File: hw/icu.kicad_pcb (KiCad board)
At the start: 2 copper layers, 60 x 90 mm, 105 parts, among them J1001 ARM_JTAG_SWD_HEADER_10_PINSMD, J101 AMPSEAL_8_POS_VERT_BLACK_SEAL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, J102 AMPSEAL_23_POS_VERT_GRAY_SEAL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, U1001 MCP2551_SOIC8, U1002 LPC1549JBD64, U301 VND5050AJTR-E, U401 VND5050AJTR-E, U501 VND5050AJTR-E, U601 VND5050AJTR-E, U701 VND5050AJTR-E, U801 VND5050AJTR-E, U901 VND5050AJTR-E, X1001 XTAL_7A-12.000MAAJ-T

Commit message: hw 1.0 ready to order
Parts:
- removed F102: FUSE_MC36211_350MA, usevolt:FUSE_MC36211
- removed R101: R_75OHM, usevolt:1206
- added D1401: DIODE_RS07J-GS18, usevolt:DO219AB, F.Cu at (182.2, 52.8)
- added R1401: 10K, yageo:0603, F.Cu at (181.4, 57.0)
- added R1402: 20K, yageo:0603, F.Cu at (183.0, 57.0)
- added R907: 1K, yageo:0603, F.Cu at (166.0, 56.9)
- R902: value e1K -> 1K
- moved F101 8.21 mm to (186.9, 69.0)
- moved R1101 4.10 mm to (169.3, 57.0)
- moved R1201 4.10 mm to (173.3, 57.0)
- moved R1301 4.10 mm to (177.3, 57.0)
- moved D1101 4.10 mm to (170.1, 52.8)
- moved D1201 4.10 mm to (174.1, 52.8)
- moved D1301 4.10 mm to (178.1, 52.8)
- moved R1102 4.10 mm to (170.9, 57.0)
- moved R1202 4.10 mm to (174.9, 57.0)
- moved R1302 4.10 mm to (178.9, 57.0)
- moved X1001 0.94 mm to (150.0, 108.3)
- moved C1008 0.94 mm to (147.3, 106.4)
- moved eC1009 0.94 mm to (147.3, 110.0)
- renumbered C1009 to eC1009
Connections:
- J102 pad 23: Net-(F102-PadP$2) -> /5V_OUT
- J102 pad 4: /Sheet5A7E031D/VIN -> /lpc1549/DIN4
- J102 pad 5: /Sheet5A7E2A6D/VIN -> /Sheet5A7E031D/VIN
- J102 pad 6: /Sheet5A7E34B9/VIN -> /Sheet5A7E2A6D/VIN
- J102 pad 7: Net-(J102-Pad7) -> /Sheet5A7E34B9/VIN
- J102 pad 8: /5V_OUT -> /Sheet5A8C5347/VIN
- U1002 pad P$1: /lpc1549/OUT2_SENSE -> Net-(R904-Pad1)
- U1002 pad P$10: /Sheet5A7B341A/IN1 -> /Sheet5A7B4C12/IN2
- U1002 pad P$11: /lpc1549/AIN3 -> /lpc1549/OUT6_SENSE
- U1002 pad P$12: (no net) -> /lpc1549/OUT7_SENSE
- U1002 pad P$15: Net-(R904-Pad1) -> (no net)
- U1002 pad P$16: Net-(R905-Pad1) -> /Sheet5A7B753C/IN2
- U1002 pad P$17: /Sheet5A7B577D/IN1 -> /Sheet5A7B753C/IN1
- U1002 pad P$19: /Sheet5A7B577D/IN2 -> /Sheet5A7B577D/IN1
- U1002 pad P$2: /Sheet5A7B2C1A/IN2 -> /Sheet5A7B341A/IN2
- U1002 pad P$23: Net-(R906-Pad1) -> (no net)
- U1002 pad P$24: /Sheet5A7B753C/IN1 -> /Sheet5A7B577D/IN2
- U1002 pad P$29: /lpc1549/OUT4_SENSE -> (no net)
- U1002 pad P$3: /lpc1549/OUT1_SENSE -> /lpc1549/AIN4
- U1002 pad P$30: /Sheet5A7B341A/IN2 -> /Sheet5A7B4C12/IN1
- U1002 pad P$31: /lpc1549/OUT6_SENSE -> /lpc1549/OUT3_SENSE
- U1002 pad P$32: /lpc1549/OUT7_SENSE -> /lpc1549/OUT4_SENSE
- U1002 pad P$33: (no net) -> /lpc1549/OUT2_SENSE
- U1002 pad P$34: (no net) -> /lpc1549/OUT1_SENSE
- U1002 pad P$4: /lpc1549/OUT3_SENSE -> /lpc1549/AIN3
- U1002 pad P$5: /Sheet5A7B1579/IN1 -> /Sheet5A7B341A/IN1
- U1002 pad P$51: (no net) -> Net-(R907-Pad2)
- U1002 pad P$53: /Sheet5A7B3FAC/IN1 -> /Sheet5A7B1579/IN2
- U1002 pad P$58: /Sheet5A7B3FAC/IN2 -> /Sheet5A7B1579/IN1
- U1002 pad P$6: /Sheet5A7B1579/IN2 -> /Sheet5A7B3FAC/IN2
- U1002 pad P$61: /Sheet5A7B4C12/IN1 -> /Sheet5A7B2C1A/IN2
- U1002 pad P$62: /Sheet5A7B753C/IN2 -> Net-(R906-Pad1)
- U1002 pad P$63: (no net) -> Net-(R905-Pad1)
- U1002 pad P$64: /Sheet5A7B4C12/IN2 -> /Sheet5A7B2C1A/IN1
- U1002 pad P$7: /Sheet5A7B2C1A/IN1 -> /Sheet5A7B3FAC/IN1
- U1002 pad P$8: /lpc1549/AIN1 -> /lpc1549/AIN2
- U1002 pad P$9: /lpc1549/AIN2 -> /lpc1549/AIN1
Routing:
- net GND: track 98.4 -> 658.2 mm, vias 47 -> 96
- net /lpc1549/AIN4: track 0.00 -> 117.1 mm, vias 0 -> 2
- net /lpc1549/AIN3: track 3.20 -> 108.9 mm, vias 0 -> 2
- net /lpc1549/AIN2: track 3.20 -> 103.3 mm, vias 0 -> 2
- net Net-(R906-Pad1): track 0.00 -> 95.5 mm, vias 0 -> 2
- net Net-(R907-Pad2): track 0.00 -> 95.0 mm, vias 0 -> 2
- net /lpc1549/AIN1: track 3.20 -> 97.2 mm, vias 0 -> 2
- net Net-(R905-Pad1): track 0.00 -> 92.2 mm, vias 0 -> 2
- net Net-(R904-Pad1): track 0.00 -> 88.8 mm, vias 0 -> 2
- net /lpc1549/OUT7_SENSE: track 10.5 -> 65.7 mm, vias 0 -> 2
- net /Sheet5A7B753C/IN2: track 2.88 -> 52.4 mm, vias 0 -> 2
- net /Sheet5A7B753C/IN1: track 2.53 -> 51.8 mm, vias 0 -> 2
- net /lpc1549/OUT6_SENSE: track 10.7 -> 59.9 mm, vias 0 -> 2
- net /Sheet5A7B4C12/IN2: track 2.91 -> 51.5 mm, vias 0 -> 2
- net /Sheet5A7B577D/IN1: track 2.50 -> 49.9 mm, vias 0 -> 2
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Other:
- net class Default: clearance 0.2 -> 0.199
- rule trace_clearance: 0.2 -> 0.199

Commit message: 3.0.0 hw and gerber created
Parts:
- removed C203: 10nF, kemet:0603
- removed D301, D401, D501, D601, D701, D801, D901: DIODE_RS07J-GS18, usevolt:DO219AB
- removed R303, R403, R503, R603, R703, R803, R903: 390, yageo:0603
- removed VR202: REG_MCP1700, usevolt:SOT-23_3-PIN
- removed eC1009: 18pF, kemet:0603
- added C1: 100nF, kemet:0603, F.Cu at (162.2, 131.4)
- added C1009: 18pF, kemet:0603, F.Cu at (147.3, 110.0)
- added D1: ZENER_MM3Z3V6T1G, usevolt:SOD-323, F.Cu at (155.1, 97.8)
- added D2: ZENER_MM3Z3V6T1G, usevolt:SOD-323, F.Cu at (162.5, 97.8)
- added D3: ZENER_MM3Z3V6T1G, usevolt:SOD-323, F.Cu at (167.7, 97.8)
- added D4: ZENER_MM3Z3V6T1G, usevolt:SOD-323, F.Cu at (174.6, 97.8)
- added D5: ZENER_MM3Z3V6T1G, usevolt:SOD-323, F.Cu at (180.8, 97.8)
- added D6: ZENER_MM3Z3V6T1G, usevolt:SOD-323, F.Cu at (186.9, 97.8)
- added D7: ZENER_MM3Z3V6T1G, usevolt:SOD-323, F.Cu at (148.5, 97.8)
- added R1: 1K, yageo:0603, F.Cu at (156.2, 93.8)
- added R2: 1K, yageo:0603, F.Cu at (162.6, 93.8)
- added R3: 1K, yageo:0603, F.Cu at (169.0, 93.8)
- added R4: 1K, yageo:0603, F.Cu at (175.4, 93.8)
- added R5: 1K, yageo:0603, F.Cu at (181.8, 93.8)
- added R6: 1K, yageo:0603, F.Cu at (188.2, 93.8)
- added R7: 1K, yageo:0603, F.Cu at (149.8, 93.8)
- added VR1: REG_MCP1700, usevolt:SOT-23_3-PIN, F.Cu at (141.7, 135.7)
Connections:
- J1001 pad P$6: (no net) -> Net-(J1001-PadP$6)
- J1001 pad P$7: (no net) -> Net-(J1001-PadP$7)
- J1001 pad P$8: (no net) -> Net-(J1001-PadP$8)
- J101 pad 7: (no net) -> Net-(J101-Pad7)
- J101 pad 8: (no net) -> Net-(J101-Pad8)
- U1001 pad 5: (no net) -> Net-(U1001-Pad5)
- U1002 pad P$15: (no net) -> Net-(U1002-PadP$15)
- U1002 pad P$23: (no net) -> Net-(U1002-PadP$23)
- U1002 pad P$25: (no net) -> Net-(U1002-PadP$25)
- U1002 pad P$29: (no net) -> Net-(U1002-PadP$29)
- U1002 pad P$38: (no net) -> Net-(U1002-PadP$38)
- U1002 pad P$39: (no net) -> Net-(U1002-PadP$39)
- U1002 pad P$42: (no net) -> Net-(U1002-PadP$42)
- U1002 pad P$43: (no net) -> Net-(U1002-PadP$43)
- U1002 pad P$46: (no net) -> Net-(U1002-PadP$46)
- U1002 pad P$47: (no net) -> Net-(U1002-PadP$47)
- U1002 pad P$48: (no net) -> Net-(U1002-PadP$48)
- U1002 pad P$49: (no net) -> Net-(U1002-PadP$49)
- U1002 pad P$50: (no net) -> Net-(U1002-PadP$50)
- U1002 pad P$54: (no net) -> Net-(U1002-PadP$54)
- U301 pad 6: (no net) -> Net-(U301-Pad6)
- U401 pad 6: (no net) -> Net-(U401-Pad6)
- U501 pad 6: (no net) -> Net-(U501-Pad6)
- U601 pad 6: (no net) -> Net-(U601-Pad6)
- U701 pad 6: (no net) -> Net-(U701-Pad6)
- U801 pad 6: (no net) -> Net-(U801-Pad6)
- U901 pad 6: (no net) -> Net-(U901-Pad6)
- VR201 pad 2: (no net) -> Net-(VR201-Pad2)
- VR201 pad 3: (no net) -> Net-(VR201-Pad3)
- VR201 pad 5: (no net) -> Net-(VR201-Pad5)
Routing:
- net +3V3: track 230.6 -> 177.2 mm, vias 2 -> 0
- net GND: track 658.2 -> 681.7 mm
- net /lpc1549/OUT4_SENSE: track 39.7 -> 41.0 mm
- net /lpc1549/OUT7_SENSE: track 65.7 -> 67.0 mm
- net /lpc1549/OUT2_SENSE: track 33.8 -> 35.1 mm
- net /lpc1549/OUT5_SENSE: track 44.9 -> 46.1 mm
- net /lpc1549/OUT6_SENSE: track 59.9 -> 61.1 mm
- net /lpc1549/OUT3_SENSE: track 38.7 -> 39.8 mm
- net /lpc1549/OUT1_SENSE: track 31.9 -> 32.9 mm
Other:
- board text added: "UW ISB 3.0 Usevolt Oy"
- board text removed: "UW ISB 1.0 Usevolt Oy"

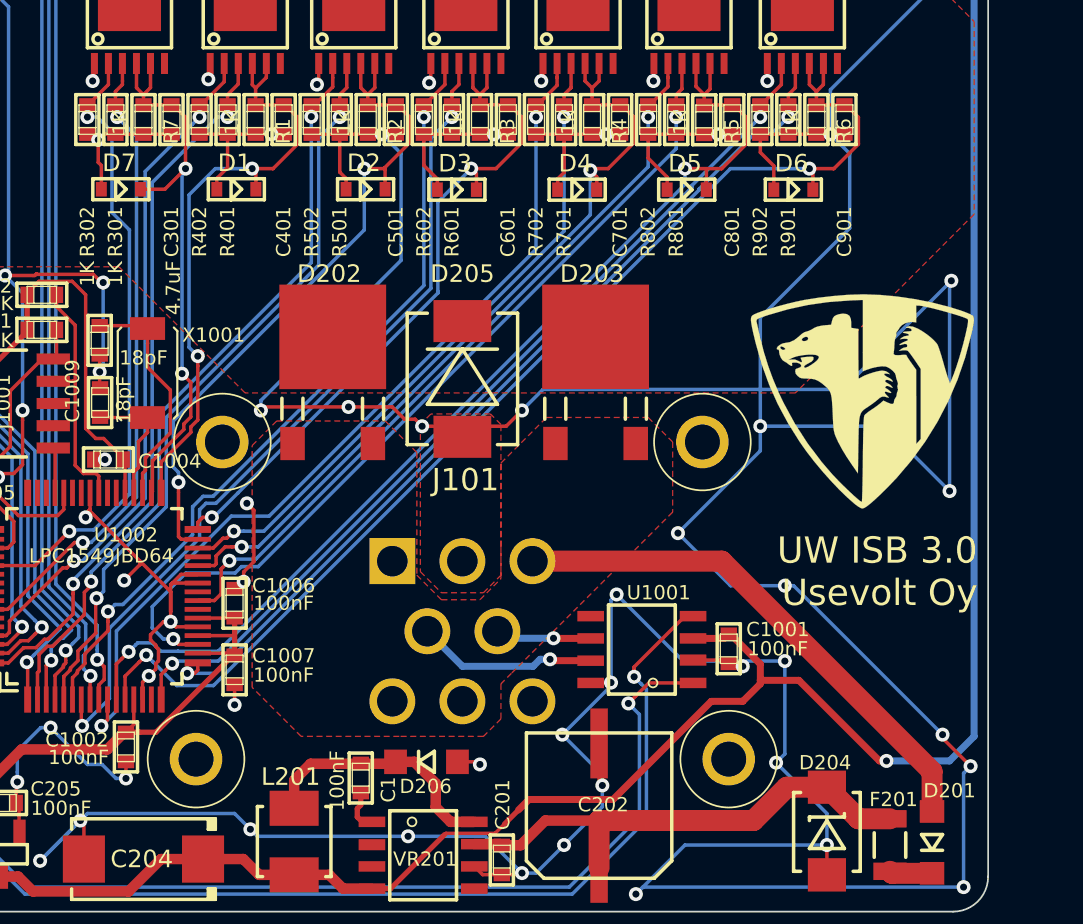
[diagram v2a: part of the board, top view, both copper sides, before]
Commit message: hw 3.1 silkscreen modifications
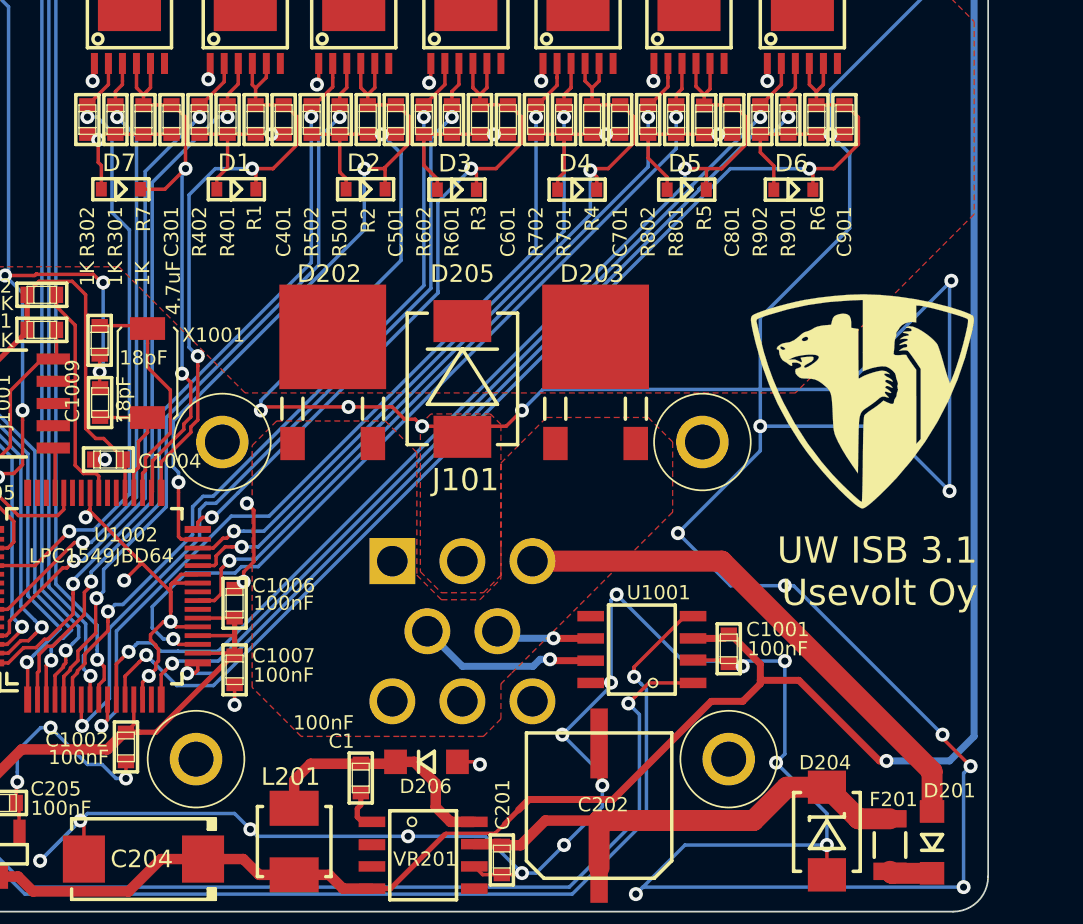
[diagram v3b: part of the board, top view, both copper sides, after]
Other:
- board text added: "UW ISB 3.1 Usevolt Oy"
- board text removed: "UW ISB 3.0 Usevolt Oy"
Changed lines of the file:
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@@
     (at 162.2 131.375 270)
     (attr smd)
-    (fp_text reference C1 (at 0.6604 -1.5748 270) (layer F.SilkS)
-      (effects (font (size 0.8128 0.8128) (thickness 0.0762)))
-    )
-    (fp_text value 100nF (at 0.1524 1.3462 270) (layer F.SilkS)
+    (fp_text reference C1 (at -2.1 1.1) (layer F.SilkS)
+      (effects (font (size 0.8128 0.8128) (thickness 0.0762)))
+    )
+    (fp_text value 100nF (at -3.15 2.125) (layer F.SilkS)
       (effects (font (size 0.8128 0.8128) (thickness 0.0762)))
     )
@@
     (at 156.2 93.8 270)
     (attr smd)
-    (fp_text reference R1 (at 0.6604 -1.5748 270) (layer F.SilkS)
-      (effects (font (size 0.8128 0.8128) (thickness 0.0762)))
-    )
-    (fp_text value 1K (at 0.1524 1.3462 270) (layer F.SilkS)
+    (fp_text reference R1 (at 5.6 0.075 270) (layer F.SilkS)
+      (effects (font (size 0.8128 0.8128) (thickness 0.0762)))
+    )
+    (fp_text value 1K (at 7.875 0.125 270) (layer F.SilkS) hide
       (effects (font (size 0.8128 0.8128) (thickness 0.0762)))
     )
@@
     (at 162.6 93.8 270)
     (attr smd)
-    (fp_text reference R2 (at 0.6604 -1.5748 270) (layer F.SilkS)
-      (effects (font (size 0.8128 0.8128) (thickness 0.0762)))
-    )
-    (fp_text value 1K (at 0.1524 1.3462 270) (layer F.SilkS)
+    (fp_text reference R2 (at 5.75 -0.025 270) (layer F.SilkS)
+      (effects (font (size 0.8128 0.8128) (thickness 0.0762)))
+    )
+    (fp_text value 1K (at 0.1524 1.3462 270) (layer F.SilkS) hide
       (effects (font (size 0.8128 0.8128) (thickness 0.0762)))
     )
@@
     (at 169 93.8 270)
     (attr smd)
-    (fp_text reference R3 (at 0.6604 -1.5748 270) (layer F.SilkS)
-      (effects (font (size 0.8128 0.8128) (thickness 0.0762)))
-    )
-    (fp_text value 1K (at 0.1524 1.3462 270) (layer F.SilkS)
+    (fp_text reference R3 (at 5.625 0.075 270) (layer F.SilkS)
+      (effects (font (size 0.8128 0.8128) (thickness 0.0762)))
+    )
+    (fp_text value 1K (at 0.1524 1.3462 270) (layer F.SilkS) hide
       (effects (font (size 0.8128 0.8128) (thickness 0.0762)))
     )
@@
     (at 175.4 93.8 270)
     (attr smd)
-    (fp_text reference R4 (at 0.6604 -1.5748 270) (layer F.SilkS)
-      (effects (font (size 0.8128 0.8128) (thickness 0.0762)))
-    )
-    (fp_text value 1K (at 0.1524 1.3462 270) (layer F.SilkS)
+    (fp_text reference R4 (at 5.65 0 270) (layer F.SilkS)
+      (effects (font (size 0.8128 0.8128) (thickness 0.0762)))
+    )
+    (fp_text value 1K (at 0.1524 1.3462 270) (layer F.SilkS) hide
       (effects (font (size 0.8128 0.8128) (thickness 0.0762)))
     )
@@
     (at 181.8 93.8118 270)
     (attr smd)
-    (fp_text reference R5 (at 0.6604 -1.5748 270) (layer F.SilkS)
-      (effects (font (size 0.8128 0.8128) (thickness 0.0762)))
-    )
-    (fp_text value 1K (at 0.1524 1.3462 270) (layer F.SilkS)
+    (fp_text reference R5 (at 5.5882 0 270) (layer F.SilkS)
+      (effects (font (size 0.8128 0.8128) (thickness 0.0762)))
+    )
+    (fp_text value 1K (at 0.1524 1.3462 270) (layer F.SilkS) hide
       (effects (font (size 0.8128 0.8128) (thickness 0.0762)))
     )
@@
     (at 188.2 93.8 270)
     (attr smd)
-    (fp_text reference R6 (at 0.6604 -1.5748 270) (layer F.SilkS)
-      (effects (font (size 0.8128 0.8128) (thickness 0.0762)))
-    )
-    (fp_text value 1K (at 0.1524 1.3462 270) (layer F.SilkS)
+    (fp_text reference R6 (at 5.625 -0.1 270) (layer F.SilkS)
+      (effects (font (size 0.8128 0.8128) (thickness 0.0762)))
+    )
+    (fp_text value 1K (at 0.1524 1.3462 270) (layer F.SilkS) hide
       (effects (font (size 0.8128 0.8128) (thickness 0.0762)))
     )
@@
     (at 149.8 93.8 270)
     (attr smd)
-    (fp_text reference R7 (at 0.6604 -1.5748 270) (layer F.SilkS)
-      (effects (font (size 0.8128 0.8128) (thickness 0.0762)))
-    )
-    (fp_text value 1K (at 0.1524 1.3462 270) (layer F.SilkS)
+    (fp_text reference R7 (at 5.675 0 270) (layer F.SilkS)
+      (effects (font (size 0.8128 0.8128) (thickness 0.0762)))
+    )
+    (fp_text value 1K (at 8.8 0.05 270) (layer F.SilkS)
       (effects (font (size 0.8128 0.8128) (thickness 0.0762)))
     )
@@
     (arrow2b (pts (xy 209.747154 49.003578) (xy 210.333575 50.130082)))
   )
-  (gr_text "UW ISB 3.0\nUsevolt Oy" (at 197.4 119.6) (layer F.SilkS)
+  (gr_text "UW ISB 3.1\nUsevolt Oy" (at 197.4 119.6) (layer F.SilkS)
     (effects (font (size 1.5 1.5) (thickness 0.3)) (justify right))
   )

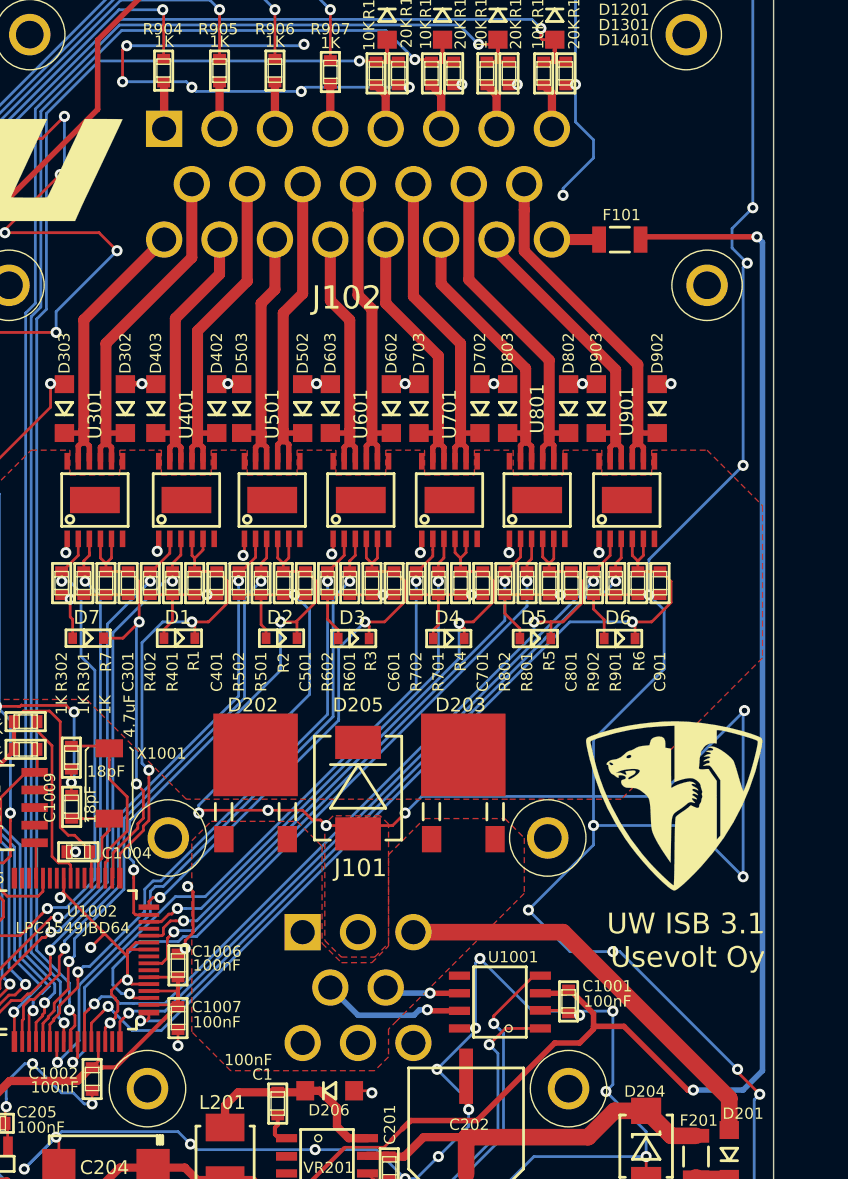
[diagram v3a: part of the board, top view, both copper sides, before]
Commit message: pcb 3.2.0 created, with 12V supply for sensors
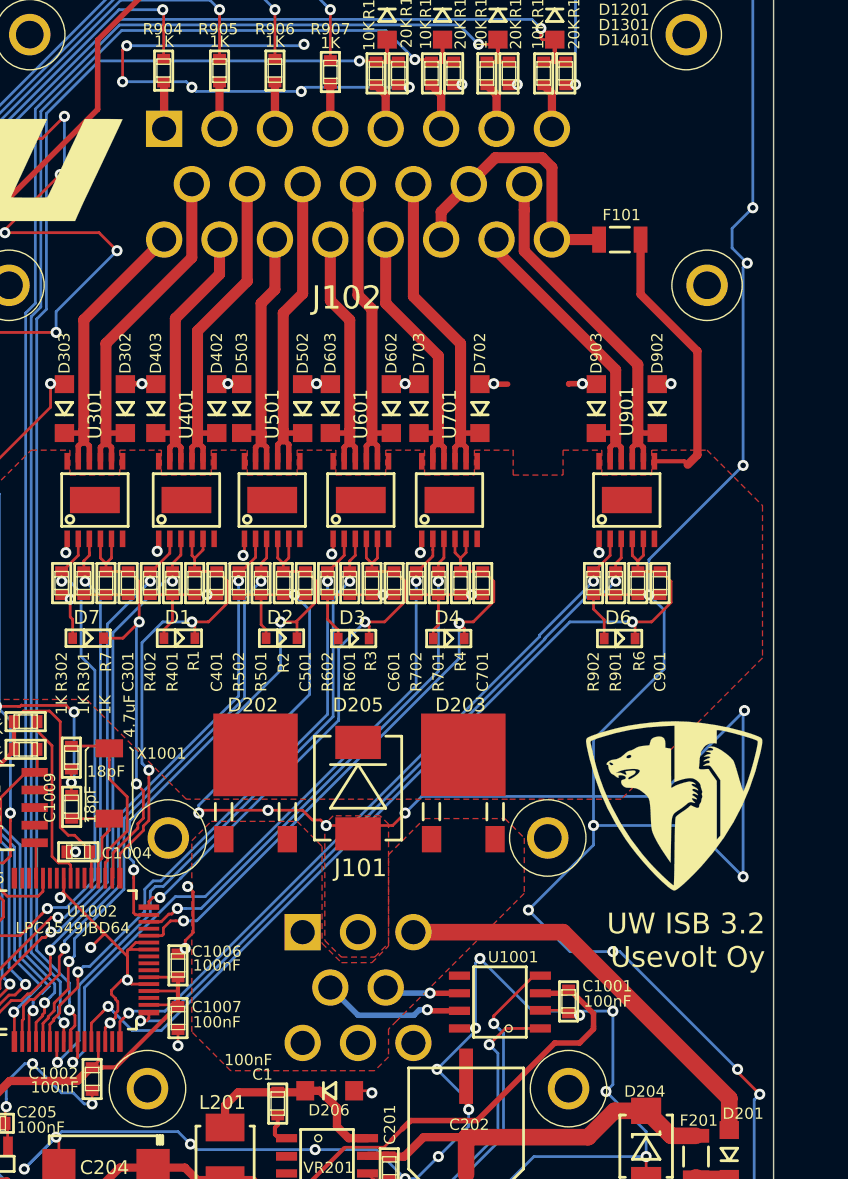
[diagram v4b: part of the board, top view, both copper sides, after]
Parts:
- removed C801: 4.7uF, kemet:0603
- removed D5: ZENER_MM3Z3V6T1G, usevolt:SOD-323
- removed D802, D803: DIODE_RS07J-GS18, usevolt:DO219AB
- removed R5, R801, R802: 1K, yageo:0603
- removed U801: VND5050AJTR-E, usevolt:PowerSSO-12
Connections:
- F101 pad P$1: +5V -> VDD
- F101 pad P$2: /5V_OUT -> /12V_OUT
- J102 pad 14: /Sheet5A7B577D/OUT1 -> /12V_OUT
- J102 pad 21: /Sheet5A7B577D/OUT2 -> /12V_OUT
- J102 pad 23: /5V_OUT -> /12V_OUT
- U1002 pad P$11: /lpc1549/OUT6_SENSE -> Net-(U1002-PadP$11)
- U1002 pad P$19: /Sheet5A7B577D/IN1 -> Net-(U1002-PadP$19)
- U1002 pad P$24: /Sheet5A7B577D/IN2 -> Net-(U1002-PadP$24)
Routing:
- net +5V: track 139.3 -> 55.7 mm, vias 2 -> 0
- net /lpc1549/OUT6_SENSE: track 61.1 -> 0.00 mm, vias 2 -> 0
- net /Sheet5A7B577D/IN1: track 49.9 -> 0.00 mm, vias 2 -> 0
- net /Sheet5A7B577D/IN2: track 43.2 -> 0.00 mm, vias 2 -> 0
- net /Sheet5A7B577D/OUT1: track 25.6 -> 0.00 mm
- net /Sheet5A7B577D/OUT2: track 21.7 -> 0.00 mm
- net VDD: track 0.00 -> 20.7 mm
- net /12V_OUT: track 0.00 -> 20.6 mm
- net GND: track 681.7 -> 662.8 mm, vias 96 -> 93
- net /5V_OUT: track 3.51 -> 0.00 mm
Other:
- board text added: "UW ISB 3.2 Usevolt Oy"
- board text removed: "UW ISB 3.1 Usevolt Oy"
